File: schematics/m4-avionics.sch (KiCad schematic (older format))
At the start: 39 parts, among them IC1 STM32F405RxTx, IC2 MCP2562, J1 USB, J2 USB, J3 UART, J4 CAMERA, P1 SWD_TC, Y1 26M

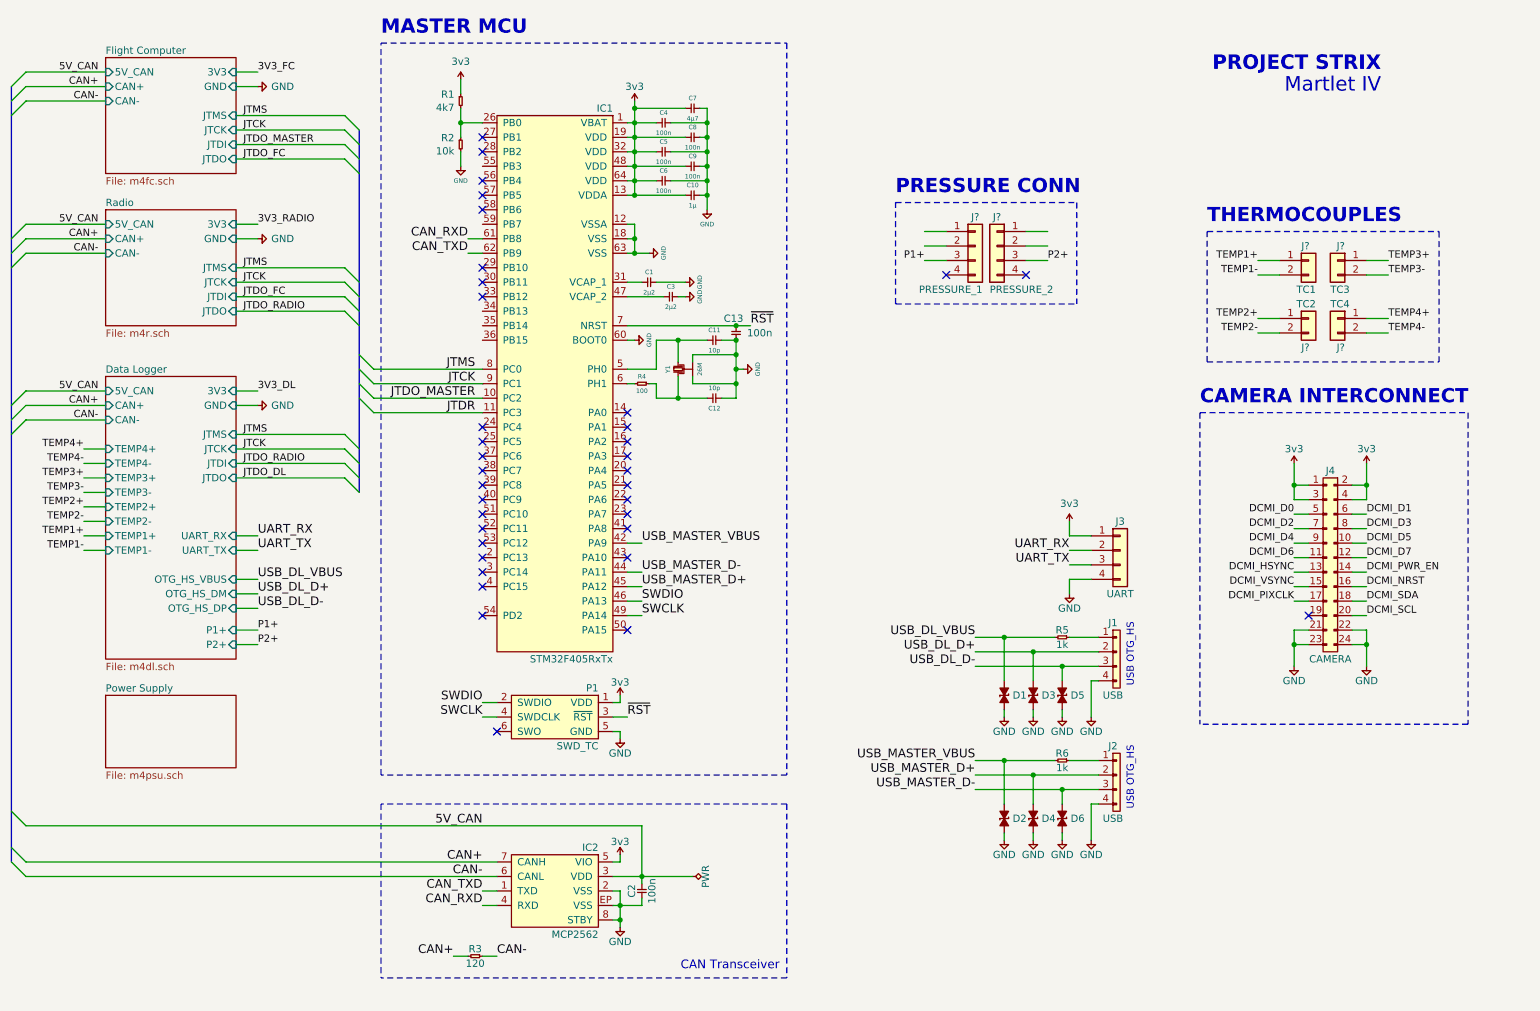
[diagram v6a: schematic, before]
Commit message: Remove pressure UART
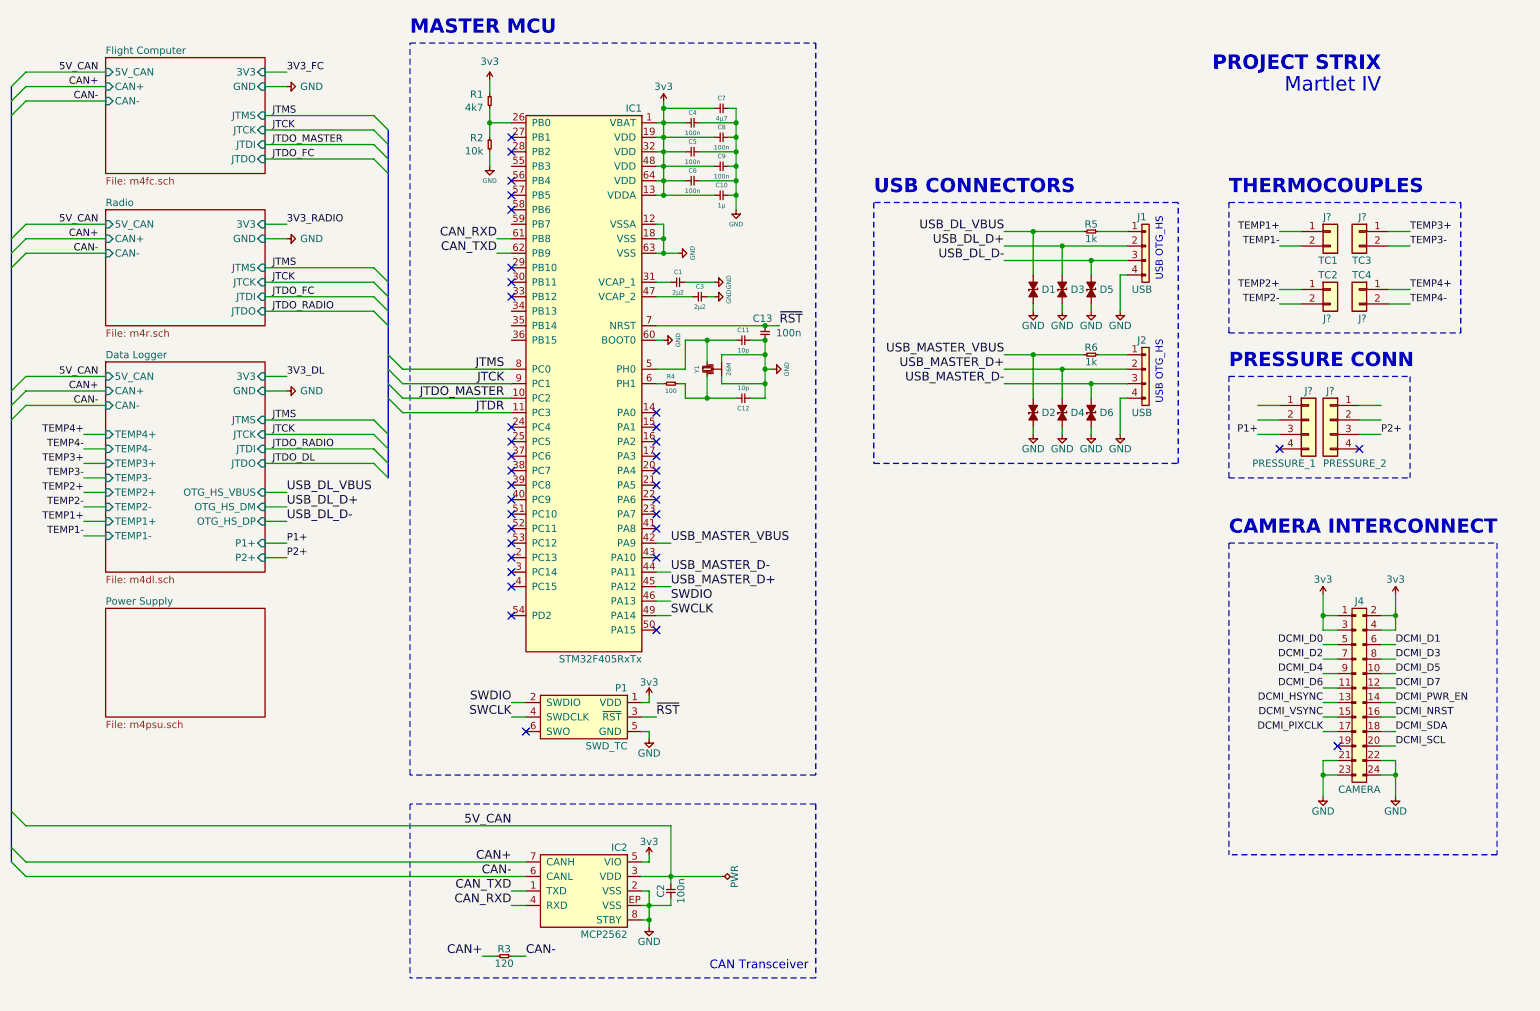
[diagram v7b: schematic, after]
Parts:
- removed J3: UART, symbol Connector_Generic:Conn_01x04
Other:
- note added: "USB CONNECTORS"
- moved on the sheet: C1, C10, C11, C12, C13, C2, C3, C4, C5, C6, C7, C8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

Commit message: Move master mcu to separate sheet
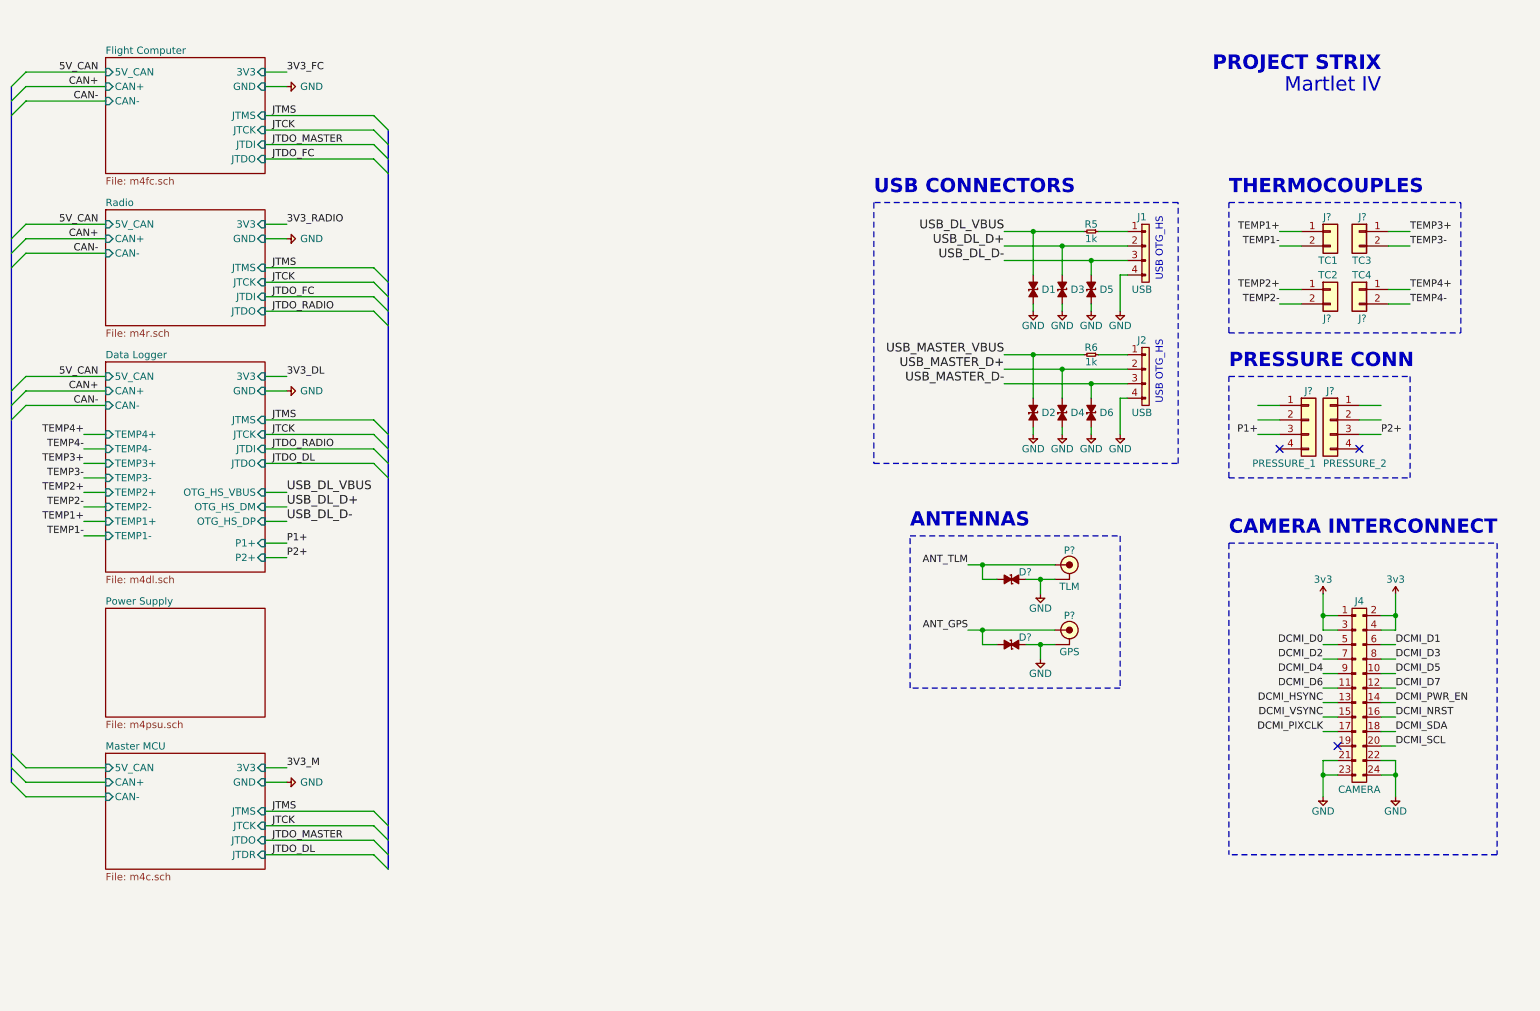
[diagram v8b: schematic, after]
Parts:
- removed C1, C3: 2µ2, agg:0402, symbol cusf-kicad:C
- removed C10: 1µ, agg:0402, symbol cusf-kicad:C
- removed C11, C12: 10p, agg:0402, symbol cusf-kicad:C
- removed C13: 100n, symbol cusf-kicad:C
- removed C2, C4, C5, C6, C8, C9: 100n, agg:0402, symbol cusf-kicad:C
- removed C7: 4µ7, agg:0402, symbol cusf-kicad:C
- removed IC1: STM32F405RxTx, agg:LQFP-64, symbol cusf-kicad:STM32F405RxTx
- removed IC2: MCP2562, agg:DFN-8-EP-MICROCHIP, symbol cusf-kicad:MCP2562
- removed P1: SWD_TC, agg:TC2030-NL, symbol cusf-kicad:SWD_TC
- removed R1: 4k7, symbol cusf-kicad:R
- removed R2: 10k, symbol cusf-kicad:R
- removed R3: 120, agg:0603, symbol cusf-kicad:R
- removed R4: 100, agg:0402, symbol cusf-kicad:R
- removed Y1: 26M, agg:XTAL-20x16, symbol cusf-kicad:SMD_XTAL
- added D? (x2): ESD_DIODE, agg:0402, symbol cusf-kicad:ESD_DIODE
- added P?: TLM, agg:SMA-EDGE, symbol cusf-kicad:COAX
- added P?: GPS, agg:SMA-EDGE, symbol cusf-kicad:COAX
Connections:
- net GND: now also D?.2, D?.2, P?.2 (GND), P?.2 (GND)
- new net ANT_GPS: D?.1, P?.1 (RF)
- new net ANT_TLM: D?.1, P?.1 (RF)
- no-connect marks 36 -> 3
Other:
- note added: "ANTENNAS"
- note removed: "CAN Transceiver"
- note removed: "MASTER MCU"
